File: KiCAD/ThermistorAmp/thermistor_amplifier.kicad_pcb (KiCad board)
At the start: 2 copper layers, 64.8 x 38.7 mm, 18 parts, among them J1 Screw_Terminal_01x02, J2 Screw_Terminal_01x03, J3 Screw_Terminal_01x02, U1 RKZE_DCDC_Conv, U2 AD623ANZ

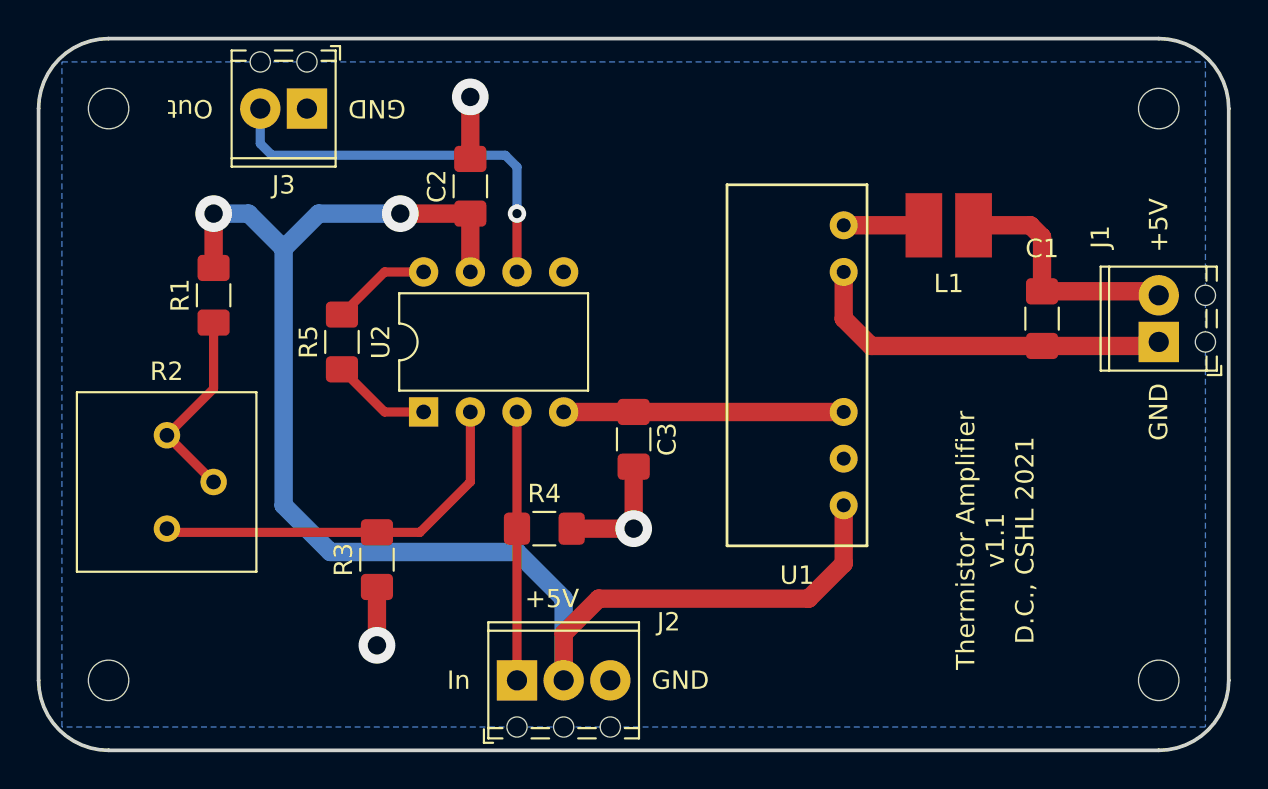
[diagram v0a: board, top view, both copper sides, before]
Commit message: Update thermistor amp to V2
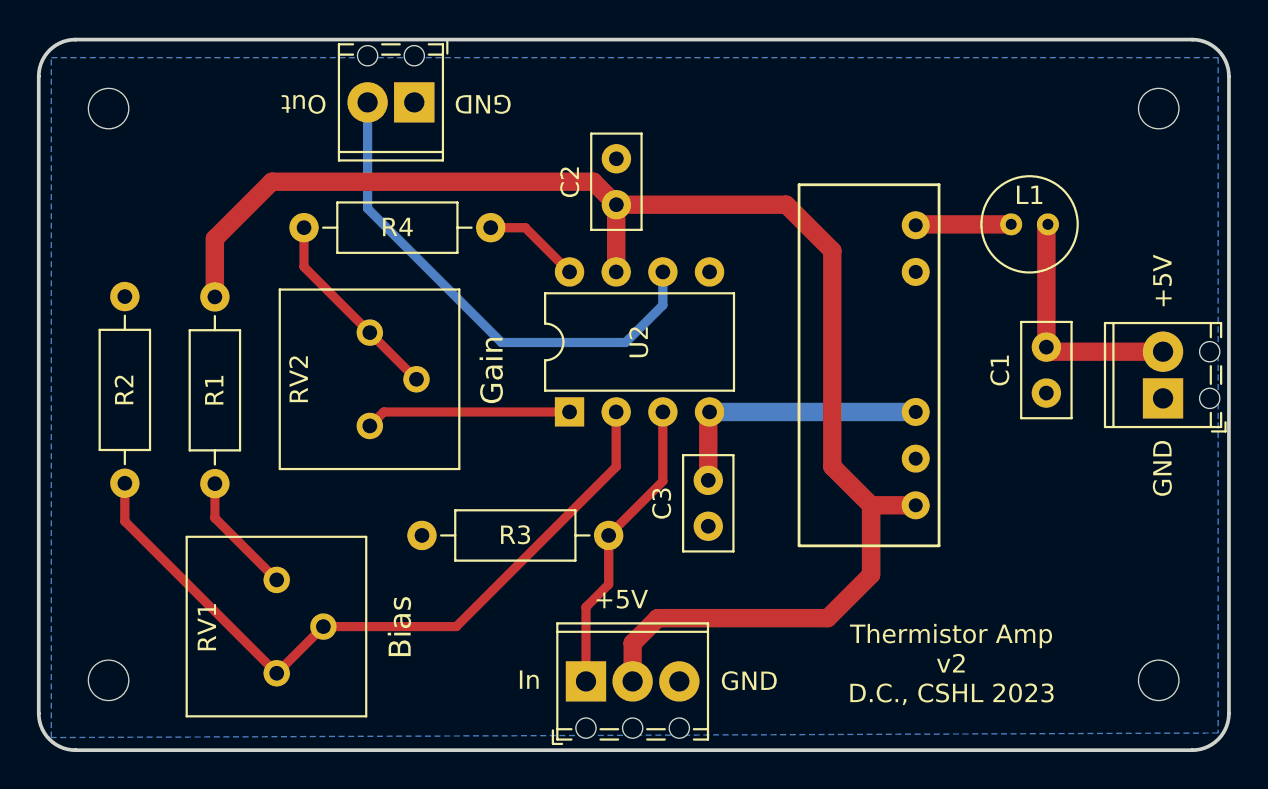
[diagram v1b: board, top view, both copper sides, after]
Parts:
- removed the R3 at (109.2, 89.3)
- added R2: 3K, Resistor_THT:R_Axial_DIN0207_L6.3mm_D2.5mm_P10.16mm_Horizontal, F.Cu at (95.5, 75.0)
- added RV2: 5K, Potentiometer_THT:Potentiometer_Bourns_3386P_Vertical, F.Cu at (108.8, 82.0)
- C1, C2, C3: footprint Capacitor_SMD:C_1206_3216Metric_Pad1.42x1.75mm_HandSolder -> Capacitor_THT:C_Disc_D5.0mm_W2.5mm_P2.50mm
- L1: footprint thermistor_amp:RecomInductor -> Capacitor_THT:C_Radial_D5.0mm_H7.0mm_P2.00mm
- R1: footprint Resistor_SMD:R_1206_3216Metric_Pad1.42x1.75mm_HandSolder -> Resistor_THT:R_Axial_DIN0207_L6.3mm_D2.5mm_P10.16mm_Horizontal
- R3: renamed from R4; footprint Resistor_SMD:R_1206_3216Metric_Pad1.42x1.75mm_HandSolder -> Resistor_THT:R_Axial_DIN0207_L6.3mm_D2.5mm_P10.16mm_Horizontal
- R4: renamed from R5; value 2.7K -> 1K; footprint Resistor_SMD:R_1206_3216Metric_Pad1.42x1.75mm_HandSolder -> Resistor_THT:R_Axial_DIN0207_L6.3mm_D2.5mm_P10.16mm_Horizontal
- RV1: renamed from R2; value 1K -> 5K
- moved R1 10.3 mm to (100.4, 85.2)
- moved RV1 9.88 mm to (103.8, 95.5)
- moved C2 8.01 mm to (122.2, 70.0)
- moved U2 7.94 mm to (119.7, 81.3)
- moved R3 6.67 mm to (111.7, 88.0), turned to 0 degrees
- moved R4 6.55 mm to (105.2, 71.2), turned to 0 degrees
- moved J3 5.85 mm to (111.2, 64.4)
- moved C3 4.63 mm to (127.2, 85.0)
- moved C1 4.06 mm to (145.7, 80.2)
- moved U1 3.92 mm to (136.0, 78.7)
- moved J2 3.76 mm to (120.6, 95.9)
- moved L1 3.40 mm to (143.7, 71.1)
- moved J1 3.08 mm to (152.0, 80.5)
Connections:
- R4 pad 1: Net-(R5-Pad1) -> Net-(R4-Pad1)
- RV1 pad 1: Net-(R2-Pad1) -> Net-(R2-Pad2)
- RV1 pad 2: Net-(R1-Pad1) -> Net-(R2-Pad2)
- U2 pad 1: Net-(R5-Pad1) -> Net-(RV2-Pad1)
- U2 pad 2: Net-(R2-Pad1) -> Net-(R2-Pad2)
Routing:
- net Net-(R2-Pad2): track 0.00 -> 39.9 mm
- net Earth: track 33.7 -> 0.35 mm, vias 3 -> 0
- net Net-(R2-Pad1): track 21.5 -> 0.00 mm
- net Net-(RV2-Pad1): track 0.00 -> 11.2 mm
- net Net-(R4-Pad1): track 0.00 -> 10.8 mm
- net Net-(R5-Pad1): track 5.41 -> 0.00 mm
- net Net-(J3-Pad2): track 22.1 -> 27.5 mm, vias 1 -> 0
- net Net-(R1-Pad1): track 10.8 -> 6.63 mm
- net Net-(L1-Pad1): track 4.37 -> 5.22 mm
- net +5V: track 80.0 -> 80.8 mm, vias 2 -> 0
- net Net-(C1-Pad2): track 14.0 -> 13.5 mm
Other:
- outline, holes or cut-outs redrawn
- net class Default removed
- board text added: "Bias"
- board text added: "Gain"
- board text added: "Thermistor Amp v2 D.C., CSHL 2023"
- board text removed: "Thermistor Amplifier v1.1 D.C., CSHL 2021"
